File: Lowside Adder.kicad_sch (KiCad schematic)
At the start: 6 parts, among them U10 VNL5090, U11 VNL5090, U12 VNL5090, U9 VNL5090

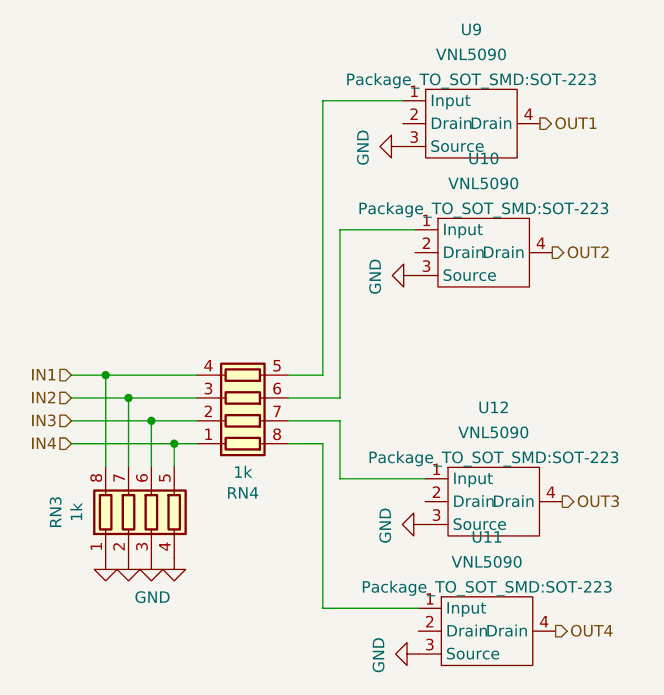
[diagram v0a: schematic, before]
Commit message: Modified IGBTs and routed smart coils
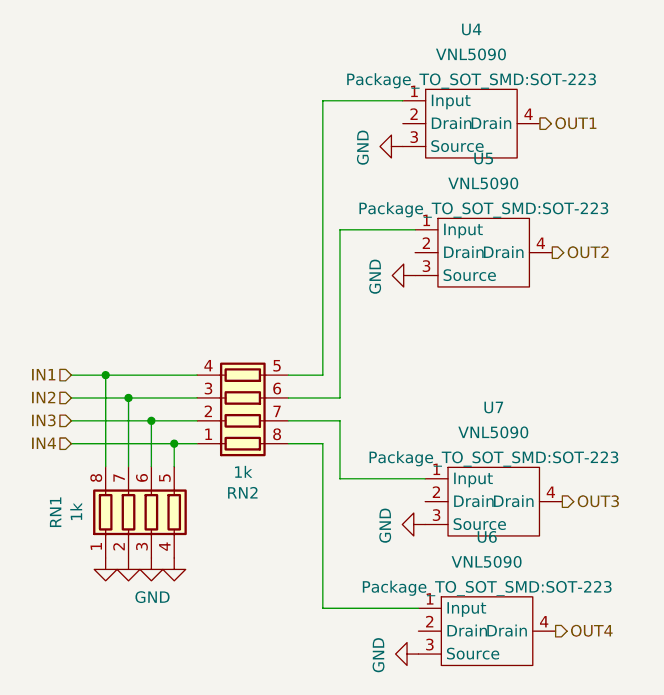
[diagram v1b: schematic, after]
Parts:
- renumbered RN3 to RN1, RN4 to RN2, U9 to U4, U10 to U5, U11 to U6, U12 to U7
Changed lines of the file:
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@@
   (symbol (lib_id "Simon:VNL5090") (at 135.9845 65.1359 0)
     (in_bom yes) (on_board yes) (fields_autoplaced)
-    (property "Reference" "U10" (id 0) (at 135.9845 57.2512 0))
+    (property "Reference" "U5" (id 0) (at 135.9845 57.2512 0))
     (property "Value" "VNL5090" (id 1) (at 135.9845 60.0263 0))
     (property "Footprint" "Package_TO_SOT_SMD:SOT-223" (id 2) (at 135.9845 62.8014 0))
@@
   (symbol (lib_id "Simon:VNL5090") (at 137.101 92.7999 0)
     (in_bom yes) (on_board yes) (fields_autoplaced)
-    (property "Reference" "U12" (id 0) (at 137.101 84.9152 0))
+    (property "Reference" "U7" (id 0) (at 137.101 84.9152 0))
     (property "Value" "VNL5090" (id 1) (at 137.101 87.6903 0))
     (property "Footprint" "Package_TO_SOT_SMD:SOT-223" (id 2) (at 137.101 90.4654 0))
@@
   (symbol (lib_id "Device:R_Pack04") (at 109.22 83.82 270) (mirror x)
     (in_bom yes) (on_board yes)
-    (property "Reference" "RN4" (id 0) (at 109.22 94.4118 90))
+    (property "Reference" "RN2" (id 0) (at 109.22 94.4118 90))
     (property "Value" "1k" (id 1) (at 109.22 92.1004 90))
     (property "Footprint" "Resistor_SMD:R_Array_Convex_4x0603" (id 2) (at 109.22 76.835 90)
@@
   (symbol (lib_id "Simon:VNL5090") (at 134.62 50.8 0)
     (in_bom yes) (on_board yes) (fields_autoplaced)
-    (property "Reference" "U9" (id 0) (at 134.62 42.9153 0))
+    (property "Reference" "U4" (id 0) (at 134.62 42.9153 0))
     (property "Value" "VNL5090" (id 1) (at 134.62 45.6904 0))
     (property "Footprint" "Package_TO_SOT_SMD:SOT-223" (id 2) (at 134.62 48.4655 0))
@@
   (symbol (lib_id "Simon:VNL5090") (at 136.3567 107.1901 0)
     (in_bom yes) (on_board yes) (fields_autoplaced)
-    (property "Reference" "U11" (id 0) (at 136.3567 99.3054 0))
+    (property "Reference" "U6" (id 0) (at 136.3567 99.3054 0))
     (property "Value" "VNL5090" (id 1) (at 136.3567 102.0805 0))
     (property "Footprint" "Package_TO_SOT_SMD:SOT-223" (id 2) (at 136.3567 104.8556 0))
@@
   (symbol (lib_id "Device:R_Pack04") (at 99.06 96.52 0)
     (in_bom yes) (on_board yes)
-    (property "Reference" "RN3" (id 0) (at 88.4682 96.52 90))
+    (property "Reference" "RN1" (id 0) (at 88.4682 96.52 90))
     (property "Value" "1k" (id 1) (at 90.7796 96.52 90))
     (property "Footprint" "Resistor_SMD:R_Array_Convex_4x0603" (id 2) (at 106.045 96.52 90)
